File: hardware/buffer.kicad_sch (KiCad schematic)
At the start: 5 parts, among them U8 MAX4238AUT

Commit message: minor changes
pre spotkanie comiit ;DD
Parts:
- removed U8: MAX4238AUT, Package_TO_SOT_SMD:SOT-23-6, symbol Amplifier_Operational:MAX4238AUT
- added U8: TSX7191, Package_TO_SOT_SMD:SOT-23-5_HandSoldering, symbol Simulation_SPICE:OPAMP
- R38: value 330R 1% -> 3.3k 1%
- R39: value 680R 1% -> 6.8k 1%
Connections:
- net +5V: now also U8.4 (V+)
- net AIR_SENSOR: no longer C34.1
- net GND: now also U8.5 (V-)
- net at R38.2, R39.1: now also C34.1, U8.1 (+)
- net at R40.1: now also U8.2 (-), U8.3
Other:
- moved on the sheet: R38
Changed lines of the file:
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@@
   (junction (at 163.83 91.44) (diameter 0) (color 0 0 0 0)
   )
+  (junction (at 130.81 88.9) (diameter 0) (color 0 0 0 0)
+  )
   (junction (at 116.84 88.9) (diameter 0) (color 0 0 0 0)
-  )
-  (junction (at 187.96 91.44) (diameter 0) (color 0 0 0 0)
   )
   (wire (pts (xy 139.7 104.14) (xy 139.7 93.98))
@@
     (stroke (width 0) (type default) (color 0 0 0 0))
   )
-  (wire (pts (xy 157.48 91.44) (xy 163.83 91.44))
+  (wire (pts (xy 130.81 88.9) (xy 130.81 92.71))
     (stroke (width 0) (type default) (color 0 0 0 0))
   )
-  (wire (pts (xy 149.86 100.33) (xy 149.86 99.06))
+  (wire (pts (xy 157.48 91.44) (xy 163.83 91.44))
     (stroke (width 0) (type default) (color 0 0 0 0))
   )
@@
     (stroke (width 0) (type default) (color 0 0 0 0))
   )
-  (wire (pts (xy 156.21 99.06) (xy 156.21 100.33))
-    (stroke (width 0) (type default) (color 0 0 0 0))
-  )
   (wire (pts (xy 116.84 97.79) (xy 116.84 110.49))
-    (stroke (width 0) (type default) (color 0 0 0 0))
-  )
-  (wire (pts (xy 187.96 102.87) (xy 187.96 111.76))
     (stroke (width 0) (type default) (color 0 0 0 0))
   )
@@
     (stroke (width 0) (type default) (color 0 0 0 0))
   )
-  (wire (pts (xy 182.88 91.44) (xy 187.96 91.44))
-    (stroke (width 0) (type default) (color 0 0 0 0))
-  )
   (wire (pts (xy 163.83 91.44) (xy 163.83 104.14))
     (stroke (width 0) (type default) (color 0 0 0 0))
   )
-  (wire (pts (xy 116.84 87.63) (xy 116.84 88.9))
+  (wire (pts (xy 130.81 88.9) (xy 116.84 88.9))
+    (stroke (width 0) (type default) (color 0 0 0 0))
+  )
+  (wire (pts (xy 116.84 86.36) (xy 116.84 88.9))
+    (stroke (width 0) (type default) (color 0 0 0 0))
+  )
+  (wire (pts (xy 130.81 100.33) (xy 130.81 109.22))
     (stroke (width 0) (type default) (color 0 0 0 0))
   )
@@
     (stroke (width 0) (type default) (color 0 0 0 0))
   )
-  (wire (pts (xy 116.84 80.01) (xy 116.84 69.85))
+  (wire (pts (xy 116.84 78.74) (xy 116.84 69.85))
     (stroke (width 0) (type default) (color 0 0 0 0))
   )
@@
     (stroke (width 0) (type default) (color 0 0 0 0))
   )
-  (wire (pts (xy 187.96 91.44) (xy 196.85 91.44))
+  (wire (pts (xy 182.88 91.44) (xy 196.85 91.44))
     (stroke (width 0) (type default) (color 0 0 0 0))
   )
-  (wire (pts (xy 156.21 100.33) (xy 149.86 100.33))
-    (stroke (width 0) (type default) (color 0 0 0 0))
-  )
-  (wire (pts (xy 187.96 91.44) (xy 187.96 95.25))
-    (stroke (width 0) (type default) (color 0 0 0 0))
-  )
-  (wire (pts (xy 142.24 88.9) (xy 116.84 88.9))
+  (wire (pts (xy 142.24 88.9) (xy 130.81 88.9))
     (stroke (width 0) (type default) (color 0 0 0 0))
   )
@@
     (stroke (width 0) (type default) (color 0 0 0 0))
   )
-  (text "PSE output impedance= 1kOhm" (at 80.01 90.17 0)
+  (text "PSE output impedance= 1kOhm" (at 46.99 78.74 0)
     (effects (font (size 1.27 1.27)) (justify left bottom))
   )
@@
       (effects (font (size 1.27 1.27)) (justify left))
     )
-    (property "Value" "680R 1%" (id 1) (at 119.38 95.2499 0)
+    (property "Value" "6.8k 1%" (id 1) (at 119.38 95.2499 0)
       (effects (font (size 1.27 1.27)) (justify left))
     )
@@
     (pin "2")
   )
-  (symbol (lib_id "Amplifier_Operational:MAX4238AUT") (at 149.86 91.44 0) (unit 1)
+  (symbol (lib_id "Device:C") (at 130.81 96.52 0) (unit 1)
     (in_bom yes) (on_board yes) (fields_autoplaced)
-    (property "Reference" "U8" (id 0) (at 162.56 86.741 0))
-    (property "Value" "MAX4238AUT" (id 1) (at 162.56 89.281 0))
-    (property "Footprint" "Package_TO_SOT_SMD:SOT-23-6" (id 2) (at 149.86 91.44 0)
+    (property "Reference" "C34" (id 0) (at 134.62 95.2499 0)
+      (effects (font (size 1.27 1.27)) (justify left))
+    )
+    (property "Value" "5.6n" (id 1) (at 134.62 97.7899 0)
+      (effects (font (size 1.27 1.27)) (justify left))
+    )
+    (property "Footprint" "" (id 2) (at 131.7752 100.33 0)
       (effects (font (size 1.27 1.27)) hide)
     )
-    (property "Datasheet" "http://datasheets.maximintegrated.com/en/ds/MAX4238-MAX4239.pdf" (id 3) (at 153.67 87.63 0)
+    (property "Datasheet" "~" (id 3) (at 130.81 96.52 0)
       (effects (font (size 1.27 1.27)) hide)
     )
     (pin "1")
     (pin "2")
-    (pin "3")
-    (pin "4")
-    (pin "5")
-    (pin "6")
   )
   (symbol (lib_id "Device:R") (at 179.07 91.44 90) (unit 1)
@@
     (pin "2")
   )
-  (symbol (lib_id "power:GND") (at 187.96 111.76 0) (unit 1)
+  (symbol (lib_id "Simulation_SPICE:OPAMP") (at 149.86 91.44 0) (unit 1)
     (in_bom yes) (on_board yes) (fields_autoplaced)
-    (property "Reference" "#PWR059" (id 0) (at 187.96 118.11 0)
+    (property "Reference" "U8" (id 0) (at 160.02 86.741 0))
+    (property "Value" "TSX7191" (id 1) (at 160.02 89.281 0))
+    (property "Footprint" "Package_TO_SOT_SMD:SOT-23-5_HandSoldering" (id 2) (at 149.86 91.44 0)
       (effects (font (size 1.27 1.27)) hide)
     )
-    (property "Value" "GND" (id 1) (at 187.96 116.84 0))
-    (property "Footprint" "" (id 2) (at 187.96 111.76 0)
+    (property "Datasheet" "https://eu.mouser.com/datasheet/2/389/dm00127571-1798280.pdf" (id 3) (at 149.86 91.44 0)
       (effects (font (size 1.27 1.27)) hide)
     )
-    (property "Datasheet" "" (id 3) (at 187.96 111.76 0)
-      (effects (font (size 1.27 1.27)) hide)
+    (property "Spice_Netlist_Enabled" "Y" (id 4) (at 149.86 91.44 0)
+      (effects (font (size 1.27 1.27)) (justify left) hide)
+    )
+    (property "Spice_Primitive" "X" (id 5) (at 149.86 91.44 0)
+      (effects (font (size 1.27 1.27)) (justify left) hide)
     )
     (pin "1")
+    (pin "2")
+    (pin "3")
+    (pin "4")
+    (pin "5")
   )
   (symbol (lib_id "power:GND") (at 147.32 110.49 0) (unit 1)
@@
     (pin "1")
   )
-  (symbol (lib_id "power:+5V") (at 156.21 99.06 0) (unit 1)
+  (symbol (lib_id "power:GND") (at 130.81 109.22 0) (unit 1)
     (in_bom yes) (on_board yes) (fields_autoplaced)
-    (property "Reference" "#PWR058" (id 0) (at 156.21 102.87 0)
+    (property "Reference" "#PWR058" (id 0) (at 130.81 115.57 0)
       (effects (font (size 1.27 1.27)) hide)
     )
-    (property "Value" "+5V" (id 1) (at 156.21 93.98 0))
-    (property "Footprint" "" (id 2) (at 156.21 99.06 0)
+    (property "Value" "GND" (id 1) (at 130.81 114.3 0))
+    (property "Footprint" "" (id 2) (at 130.81 109.22 0)
       (effects (font (size 1.27 1.27)) hide)
     )
-    (property "Datasheet" "" (id 3) (at 156.21 99.06 0)
+    (property "Datasheet" "" (id 3) (at 130.81 109.22 0)
       (effects (font (size 1.27 1.27)) hide)
     )
     (pin "1")
   )
-  (symbol (lib_id "Device:R") (at 116.84 83.82 0) (unit 1)
+  (symbol (lib_id "Device:R") (at 116.84 82.55 0) (unit 1)
     (in_bom yes) (on_board yes) (fields_autoplaced)
-    (property "Reference" "R38" (id 0) (at 119.38 82.5499 0)
+    (property "Reference" "R38" (id 0) (at 119.38 81.2799 0)
       (effects (font (size 1.27 1.27)) (justify left))
     )
-    (property "Value" "330R 1%" (id 1) (at 119.38 85.0899 0)
+    (property "Value" "3.3k 1%" (id 1) (at 119.38 83.8199 0)
       (effects (font (size 1.27 1.27)) (justify left))
     )
-    (property "Footprint" "Resistor_SMD:R_0603_1608Metric" (id 2) (at 115.062 83.82 90)
+    (property "Footprint" "Resistor_SMD:R_0603_1608Metric" (id 2) (at 115.062 82.55 90)
       (effects (font (size 1.27 1.27)) hide)
     )
-    (property "Datasheet" "~" (id 3) (at 116.84 83.82 0)
+    (property "Datasheet" "~" (id 3) (at 116.84 82.55 0)
       (effects (font (size 1.27 1.27)) hide)
     )
-    (pin "1")
-    (pin "2")
-  )
-  (symbol (lib_id "Device:C") (at 187.96 99.06 0) (unit 1)
-    (in_bom yes) (on_board yes) (fields_autoplaced)
-    (property "Reference" "C34" (id 0) (at 191.77 97.7899 0)
-      (effects (font (size 1.27 1.27)) (justify left))
-    )
-    (property "Value" "5.6n" (id 1) (at 191.77 100.3299 0)
-      (effects (font (size 1.27 1.27)) (justify left))
-    )
-    (property "Footprint" "" (id 2) (at 188.9252 102.87 0)
-      (effects (font (size 1.27 1.27)) hide)
-    )
-    (property "Datasheet" "~" (id 3) (at 187.96 99.06 0)
-      (effects (font (size 1.27 1.27)) hide)
-    )

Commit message: kończymy balet na dziś
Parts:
- C34: footprint (none) -> Capacitor_SMD:C_0603_1608Metric
- R38, R39, R40: footprint Resistor_SMD:R_0603_1608Metric -> Resistor_SMD:R_0603_1608Metric_Pad0.98x0.95mm_HandSolder
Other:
- note added: "1k(sens out z)"
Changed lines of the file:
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@@
   (junction (at 116.84 88.9) (diameter 0) (color 0 0 0 0)
+  )
+  (polyline (pts (xy 95.25 68.58) (xy 95.25 72.39))
+    (stroke (width 0) (type default) (color 0 0 0 0))
   )
   (wire (pts (xy 139.7 104.14) (xy 139.7 93.98))
@@
     (stroke (width 0) (type default) (color 0 0 0 0))
   )
+  (polyline (pts (xy 105.41 72.39) (xy 105.41 68.58))
+    (stroke (width 0) (type default) (color 0 0 0 0))
+  )
   (wire (pts (xy 157.48 91.44) (xy 163.83 91.44))
     (stroke (width 0) (type default) (color 0 0 0 0))
   )
   (wire (pts (xy 116.84 88.9) (xy 116.84 90.17))
+    (stroke (width 0) (type default) (color 0 0 0 0))
+  )
+  (polyline (pts (xy 95.25 68.58) (xy 105.41 68.58))
     (stroke (width 0) (type default) (color 0 0 0 0))
   )
@@
     (stroke (width 0) (type default) (color 0 0 0 0))
   )
+  (polyline (pts (xy 95.25 72.39) (xy 105.41 72.39))
+    (stroke (width 0) (type default) (color 0 0 0 0))
+  )
   (wire (pts (xy 142.24 88.9) (xy 130.81 88.9))
     (stroke (width 0) (type default) (color 0 0 0 0))
@@
     (stroke (width 0) (type default) (color 0 0 0 0))
   )
-  (text "PSE output impedance= 1kOhm" (at 46.99 78.74 0)
+  (text "1k(sens out z)" (at 92.71 67.31 0)
+    (effects (font (size 1.27 1.27) italic) (justify left bottom))
+  )
+  (text "PSE output impedance= 1kOhm" (at 80.01 88.9 0)
     (effects (font (size 1.27 1.27)) (justify left bottom))
   )
@@
       (effects (font (size 1.27 1.27)) (justify left))
     )
-    (property "Footprint" "Resistor_SMD:R_0603_1608Metric" (id 2) (at 115.062 93.98 90)
+    (property "Footprint" "Resistor_SMD:R_0603_1608Metric_Pad0.98x0.95mm_HandSolder" (id 2) (at 115.062 93.98 90)
       (effects (font (size 1.27 1.27)) hide)
     )
@@
       (effects (font (size 1.27 1.27)) (justify left))
     )
-    (property "Footprint" "" (id 2) (at 131.7752 100.33 0)
+    (property "Footprint" "Capacitor_SMD:C_0603_1608Metric" (id 2) (at 131.7752 100.33 0)
       (effects (font (size 1.27 1.27)) hide)
     )
@@
     (property "Reference" "R40" (id 0) (at 179.07 85.09 90))
     (property "Value" "1k" (id 1) (at 179.07 87.63 90))
-    (property "Footprint" "Resistor_SMD:R_0603_1608Metric" (id 2) (at 179.07 93.218 90)
+    (property "Footprint" "Resistor_SMD:R_0603_1608Metric_Pad0.98x0.95mm_HandSolder" (id 2) (at 179.07 93.218 90)
       (effects (font (size 1.27 1.27)) hide)
     )
@@
       (effects (font (size 1.27 1.27)) (justify left))
     )
-    (property "Footprint" "Resistor_SMD:R_0603_1608Metric" (id 2) (at 115.062 82.55 90)
+    (property "Footprint" "Resistor_SMD:R_0603_1608Metric_Pad0.98x0.95mm_HandSolder" (id 2) (at 115.062 82.55 90)
       (effects (font (size 1.27 1.27)) hide)
     )

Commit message: kurde no jeszcze nie skonczylem ale sune dalej
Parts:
- C34: footprint Capacitor_SMD:C_0603_1608Metric -> Capacitor_SMD:C_0603_1608Metric_Pad1.08x0.95mm_HandSolder
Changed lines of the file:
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@@
       (effects (font (size 1.27 1.27)) (justify left))
     )
-    (property "Footprint" "Capacitor_SMD:C_0603_1608Metric" (id 2) (at 131.7752 100.33 0)
+    (property "Footprint" "Capacitor_SMD:C_0603_1608Metric_Pad1.08x0.95mm_HandSolder" (id 2) (at 131.7752 100.33 0)
       (effects (font (size 1.27 1.27)) hide)
     )

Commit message: fixed references addet tp;s mam pojutrze przejebany egzamin nara
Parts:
- added C37: 100nF, Capacitor_SMD:C_0603_1608Metric, symbol Device:C
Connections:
- net +5V: now also C37.1
- net GND: now also C37.2
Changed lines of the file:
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@@
   (junction (at 163.83 91.44) (diameter 0) (color 0 0 0 0)
   )
+  (junction (at 147.32 74.93) (diameter 0) (color 0 0 0 0)
+  )
   (junction (at 130.81 88.9) (diameter 0) (color 0 0 0 0)
   )
@@
     (stroke (width 0) (type default) (color 0 0 0 0))
   )
+  (wire (pts (xy 137.16 74.93) (xy 147.32 74.93))
+    (stroke (width 0) (type default) (color 0 0 0 0))
+  )
   (wire (pts (xy 130.81 88.9) (xy 130.81 92.71))
     (stroke (width 0) (type default) (color 0 0 0 0))
@@
     (stroke (width 0) (type default) (color 0 0 0 0))
   )
-  (wire (pts (xy 147.32 73.66) (xy 147.32 83.82))
+  (wire (pts (xy 147.32 73.66) (xy 147.32 74.93))
     (stroke (width 0) (type default) (color 0 0 0 0))
   )
@@
   )
   (wire (pts (xy 90.17 69.85) (xy 116.84 69.85))
+    (stroke (width 0) (type default) (color 0 0 0 0))
+  )
+  (wire (pts (xy 147.32 74.93) (xy 147.32 83.82))
     (stroke (width 0) (type default) (color 0 0 0 0))
   )
@@
     (pin "1")
   )
+  (symbol (lib_id "Device:C") (at 137.16 78.74 0) (unit 1)
+    (in_bom yes) (on_board yes) (fields_autoplaced)
+    (property "Reference" "C37" (id 0) (at 140.97 77.4699 0)
+      (effects (font (size 1.27 1.27)) (justify left))
+    )
+    (property "Value" "100nF" (id 1) (at 140.97 80.0099 0)
+      (effects (font (size 1.27 1.27)) (justify left))
+    )
+    (property "Footprint" "Capacitor_SMD:C_0603_1608Metric" (id 2) (at 138.1252 82.55 0)
+      (effects (font (size 1.27 1.27)) hide)
+    )
+    (property "Datasheet" "~" (id 3) (at 137.16 78.74 0)
+      (effects (font (size 1.27 1.27)) hide)
+    )
+    (pin "1")
+    (pin "2")
+  )
   (symbol (lib_id "power:GND") (at 130.81 109.22 0) (unit 1)
     (in_bom yes) (on_board yes) (fields_autoplaced)
@@
       (effects (font (size 1.27 1.27)) hide)
     )
+    (pin "1")
+  )
+  (symbol (lib_id "power:GND") (at 137.16 82.55 0) (unit 1)
+    (in_bom yes) (on_board yes) (fields_autoplaced)
+    (property "Reference" "#PWR0112" (id 0) (at 137.16 88.9 0)
+      (effects (font (size 1.27 1.27)) hide)
+    )
+    (property "Value" "GND" (id 1) (at 137.16 87.63 0))
+    (property "Footprint" "" (id 2) (at 137.16 82.55 0)
+      (effects (font (size 1.27 1.27)) hide)
+    )
+    (property "Datasheet" "" (id 3) (at 137.16 82.55 0)
+      (effects (font (size 1.27 1.27)) hide)
+    )

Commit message: L4 port
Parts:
- U8: value TSX7191 -> ${SIM.PARAMS}; Spice_Netlist_Enabled Y -> (none); Spice_Primitive X -> (none)

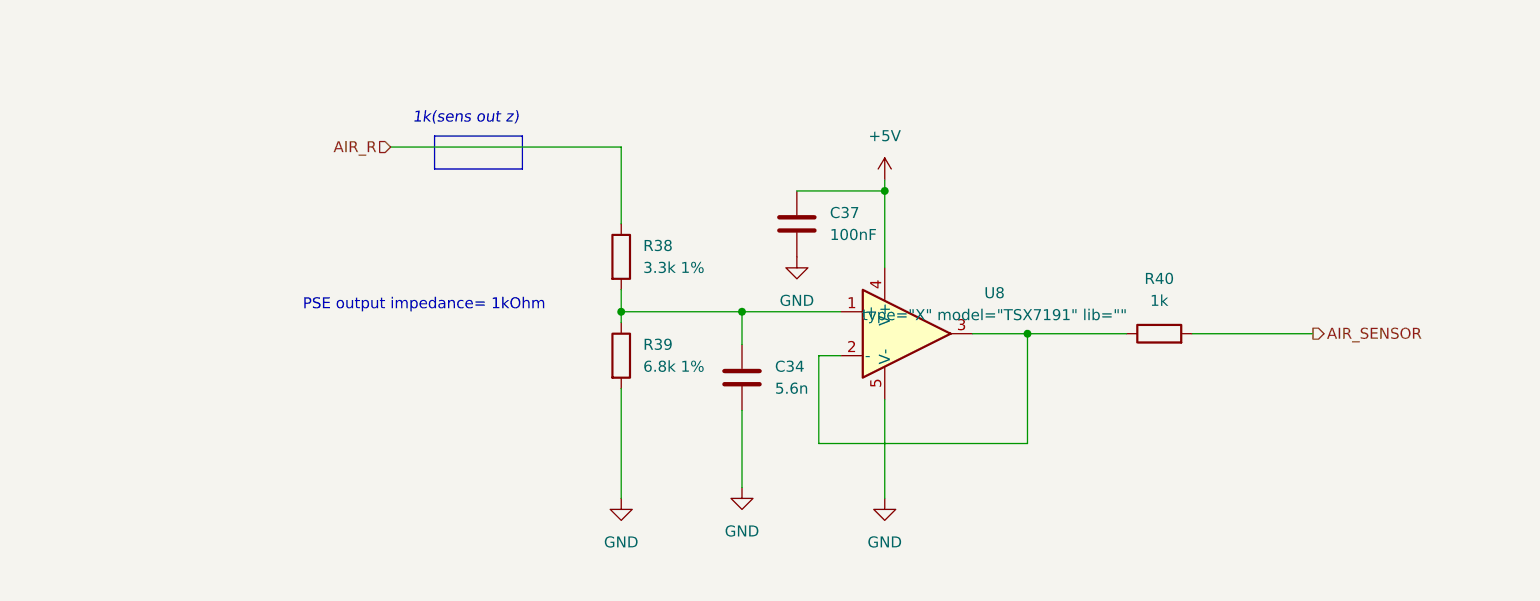
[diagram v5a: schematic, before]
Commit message: Schematic redesign for 23 rules, new pressure buffer, protection fix
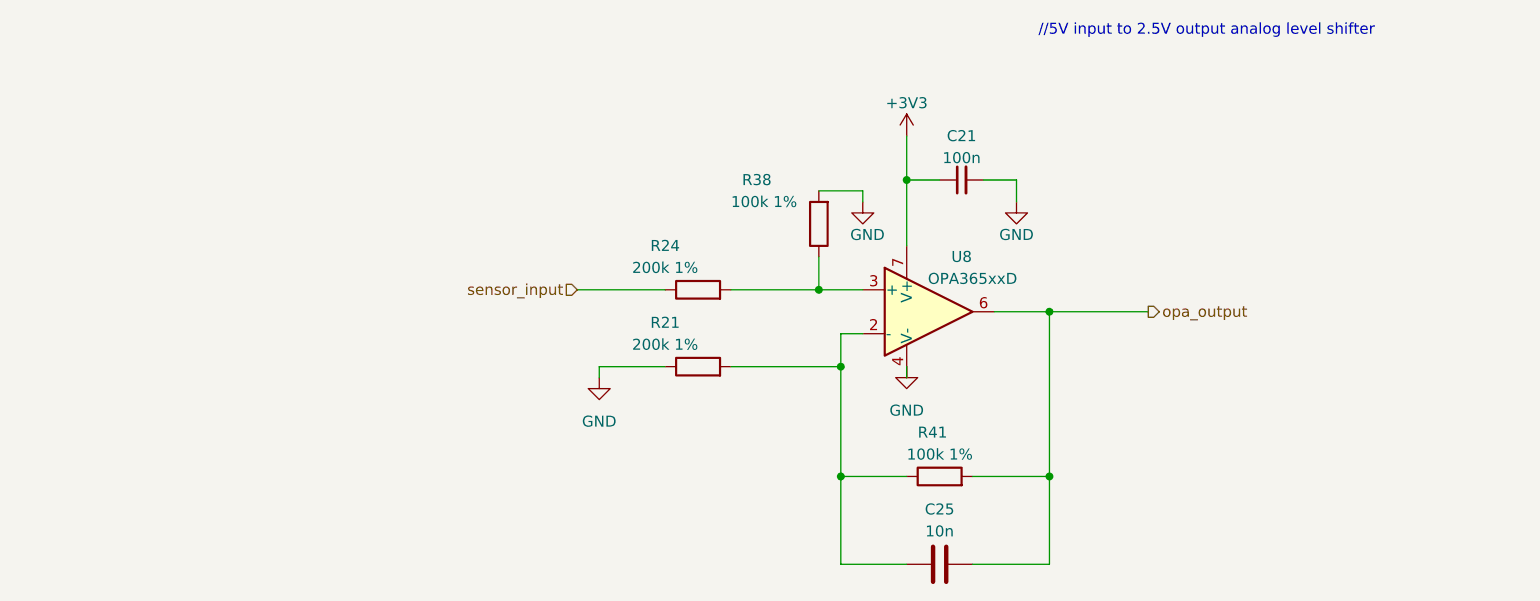
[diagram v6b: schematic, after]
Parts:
- removed C34: 5.6n, Capacitor_SMD:C_0603_1608Metric_Pad1.08x0.95mm_HandSolder, symbol Device:C
- removed C37: 100nF, Capacitor_SMD:C_0603_1608Metric, symbol Device:C
- removed R39: 6.8k 1%, Resistor_SMD:R_0603_1608Metric_Pad0.98x0.95mm_HandSolder, symbol Device:R
- removed R40: 1k, Resistor_SMD:R_0603_1608Metric_Pad0.98x0.95mm_HandSolder, symbol Device:R
- removed U8: ${SIM.PARAMS}, Package_TO_SOT_SMD:SOT-23-5_HandSoldering, symbol Simulation_SPICE:OPAMP
- added C21: 100n, Capacitor_SMD:C_0603_1608Metric_Pad1.08x0.95mm_HandSolder, symbol Device:C_Small
- added C25: 10n, Capacitor_SMD:C_0603_1608Metric_Pad1.08x0.95mm_HandSolder, symbol Device:C
- added R21, R24: 200k 1%, Resistor_SMD:R_0603_1608Metric_Pad0.98x0.95mm_HandSolder, symbol Device:R
- added R41: 100k 1%, Resistor_SMD:R_0603_1608Metric_Pad0.98x0.95mm_HandSolder, symbol Device:R
- added U8: OPA365xxD, Package_SO:SOIC-8_3.9x4.9mm_P1.27mm, symbol Amplifier_Operational:OPA365xxD
- R38: value 3.3k 1% -> 100k 1%
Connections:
- net GND: now also R38.2, C21.2, R21.1, U8.4 (V-)
- net AIR_R: no longer names the net of R38.1
- net AIR_R: now also R24.2, U8.3 (+)
- new net: C25.1, R21.2, R41.1, U8.2 (-)
- new net +3V3: C21.1, U8.7 (V+)
- new net opa_output: C25.2, R41.2, U8.6
- new net sensor_input: R24.1
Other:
- note added: "//5V input to 2.5V output analog level shifter"
- note removed: "1k(sens out z)"
- note removed: "PSE output impedance= 1kOhm"
